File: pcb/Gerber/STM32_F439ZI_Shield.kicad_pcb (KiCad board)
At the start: 2 copper layers, 70 x 133.4 mm, 128 parts, among them CN10 Conn_02x17_Odd_Even, CN7 Conn_02x10_Odd_Even, CN8 Conn_02x08_Odd_Even, CN9 Conn_02x15_Odd_Even, J1 Conn_01x02_Pin, J3 Relais_Conn, J4 Conn_01x02_Pin, J5 Conn_01x02_Pin, J6 Conn_01x02_Pin, J7 Conn_01x02_Pin, J8 Conn_01x02_Pin, K1 G6S-2, K2 G6S-2, U1 LM2904, U10 LTV-817S, U11 LTV-817S, U12 FL25L16B, U13 R-78E-5.0-1.0, U15 ACS724xLCTR-05AB, U2 MAX3485, U3 LTV-817S, U4 LTV-817S, U5 LTV-817S, U6 LTV-817S, U7 LTV-817S, U8 LTV-817S, U9 LTV-817S

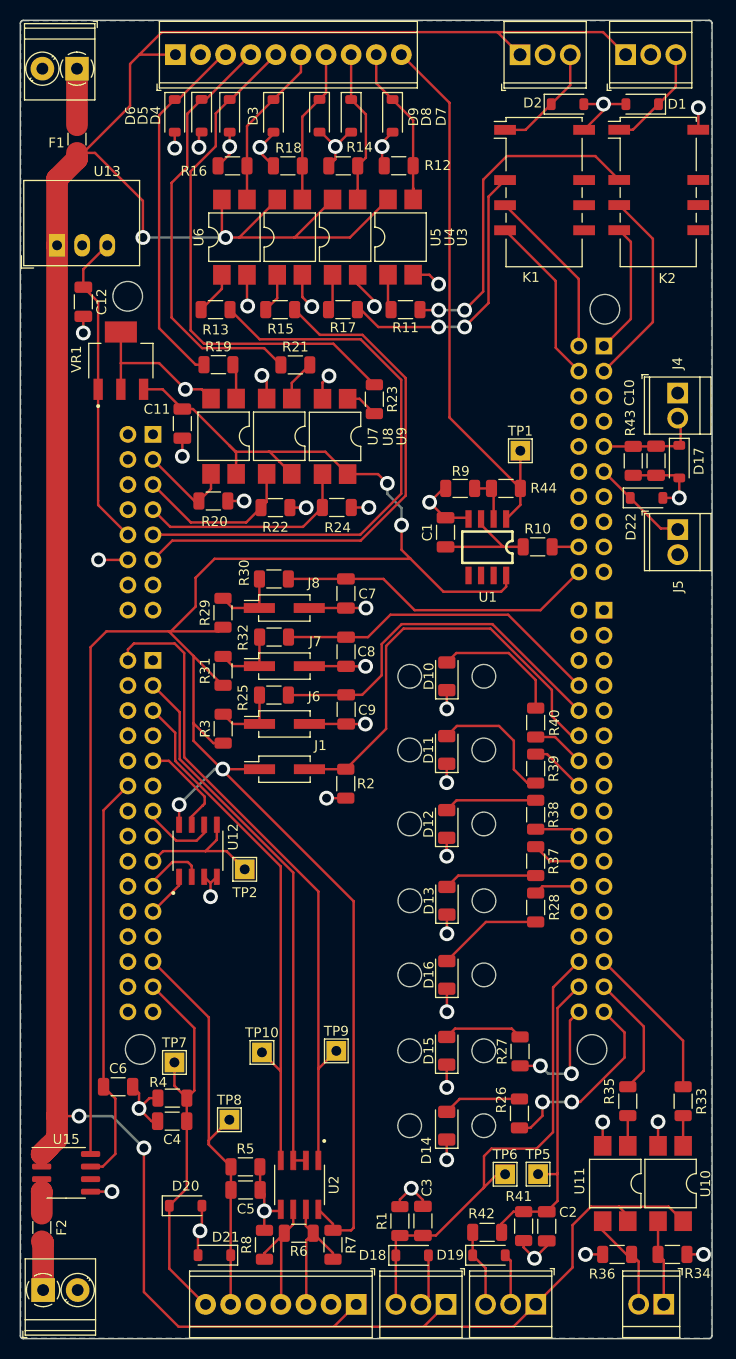
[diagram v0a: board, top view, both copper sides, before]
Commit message: finished assigning pins and creating pcb
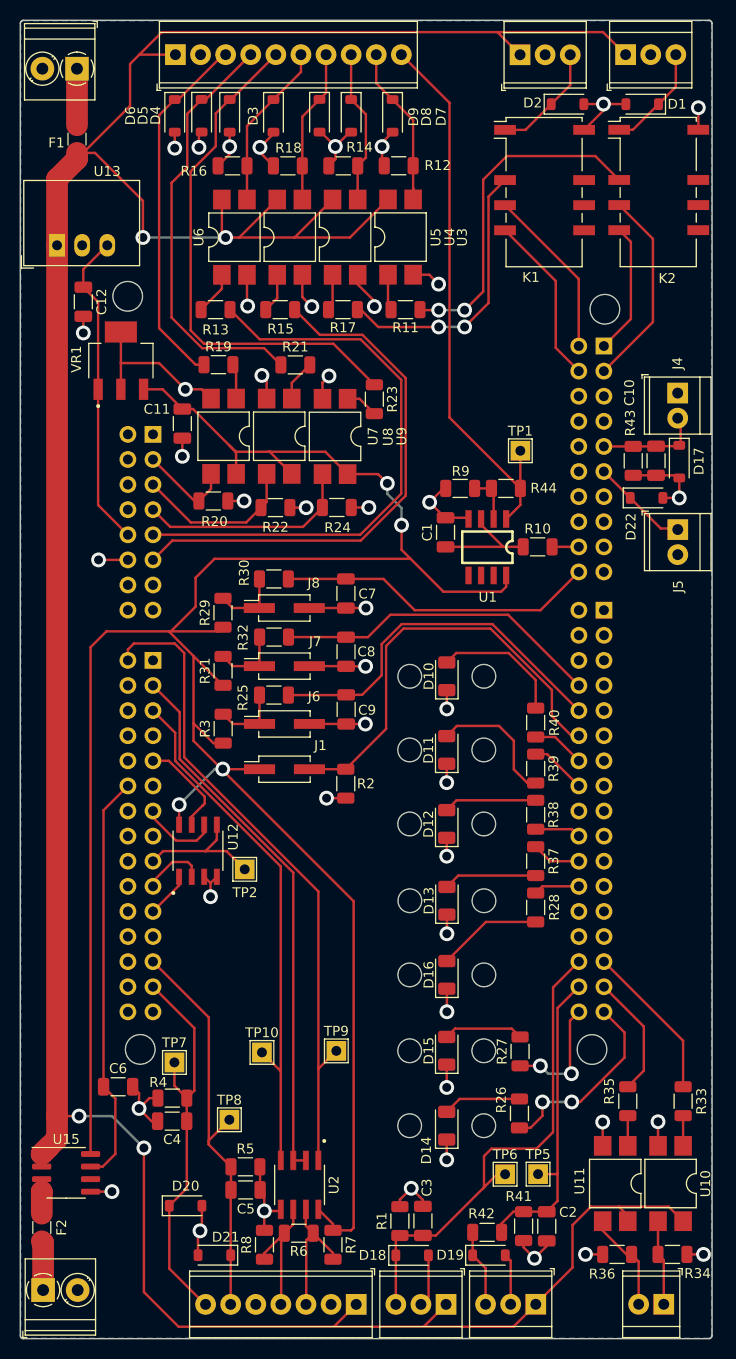
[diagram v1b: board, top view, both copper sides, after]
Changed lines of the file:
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@@
     (fp_circle (center 5.08 0) (end 6.18 0)
       (stroke (width 0.1) (type solid)) (fill none) (layer "F.Fab"))
-    (pad "1" thru_hole rect (at 0 0) (size 2.1 2.1) (drill 1.3) (layers "*.Cu" "*.Mask")
+    (pad "1" thru_hole rect (at 0 0) (size 2.1 2.1) (drill 1.1) (layers "*.Cu" "*.Mask")
       (net 1 "+24V") (pinfunction "Pin_1") (pintype "passive"))
-    (pad "2" thru_hole circle (at 2.54 0) (size 2.1 2.1) (drill 1.3) (layers "*.Cu" "*.Mask")
+    (pad "2" thru_hole circle (at 2.54 0) (size 2.1 2.1) (drill 1.1) (layers "*.Cu" "*.Mask")
       (net 2 "GND") (pinfunction "Pin_2") (pintype "passive"))
-    (pad "3" thru_hole circle (at 5.08 0) (size 2.1 2.1) (drill 1.3) (layers "*.Cu" "*.Mask")
+    (pad "3" thru_hole circle (at 5.08 0) (size 2.1 2.1) (drill 1.1) (layers "*.Cu" "*.Mask")
       (net 128 "/Endschalter/Endschalter_Hinten") (pinfunction "Pin_3") (pintype "passive"))
     (model "${KICAD6_3DMODEL_DIR}/TerminalBlock_TE-Connectivity.3dshapes/TerminalBlock_TE_282834-3_1x03_P2.54mm_Horizontal.wrl"
@@
     (fp_circle (center 2.54 0) (end 3.64 0)
       (stroke (width 0.1) (type solid)) (fill none) (layer "F.Fab"))
-    (pad "1" thru_hole rect (at 0 0 180) (size 2.1 2.1) (drill 1.3) (layers "*.Cu" "*.Mask")
+    (pad "1" thru_hole rect (at 0 0 180) (size 2.1 2.1) (drill 1.1) (layers "*.Cu" "*.Mask")
       (net 132 "/Optokoppler/Ext_Relais1_OUT") (pinfunction "Pin_1") (pintype "passive"))
-    (pad "2" thru_hole circle (at 2.54 0 180) (size 2.1 2.1) (drill 1.3) (layers "*.Cu" "*.Mask")
+    (pad "2" thru_hole circle (at 2.54 0 180) (size 2.1 2.1) (drill 1.1) (layers "*.Cu" "*.Mask")
       (net 133 "/Optokoppler/Ext_Relais2_OUT") (pinfunction "Pin_2") (pintype "passive"))
     (model "${KICAD6_3DMODEL_DIR}/TerminalBlock_TE-Connectivity.3dshapes/TerminalBlock_TE_282834-2_1x02_P2.54mm_Horizontal.wrl"
@@
     (fp_circle (center 5.08 0) (end 6.18 0)
       (stroke (width 0.1) (type solid)) (fill none) (layer "F.Fab"))
-    (pad "1" thru_hole rect (at 0 0 180) (size 2.1 2.1) (drill 1.3) (layers "*.Cu" "*.Mask")
+    (pad "1" thru_hole rect (at 0 0 180) (size 2.1 2.1) (drill 1.1) (layers "*.Cu" "*.Mask")
       (net 1 "+24V") (pinfunction "Pin_1") (pintype "passive"))
-    (pad "2" thru_hole circle (at 2.54 0 180) (size 2.1 2.1) (drill 1.3) (layers "*.Cu" "*.Mask")
+    (pad "2" thru_hole circle (at 2.54 0 180) (size 2.1 2.1) (drill 1.1) (layers "*.Cu" "*.Mask")
       (net 2 "GND") (pinfunction "Pin_2") (pintype "passive"))
-    (pad "3" thru_hole circle (at 5.08 0 180) (size 2.1 2.1) (drill 1.3) (layers "*.Cu" "*.Mask")
+    (pad "3" thru_hole circle (at 5.08 0 180) (size 2.1 2.1) (drill 1.1) (layers "*.Cu" "*.Mask")
       (net 150 "Net-(D19-K)") (pinfunction "Pin_3") (pintype "passive"))
     (model "${KICAD6_3DMODEL_DIR}/TerminalBlock_TE-Connectivity.3dshapes/TerminalBlock_TE_282834-3_1x03_P2.54mm_Horizontal.wrl"
@@
     (fp_circle (center 2.54 0) (end 3.64 0)
       (stroke (width 0.1) (type solid)) (fill none) (layer "F.Fab"))
-    (pad "1" thru_hole rect (at 0 0 270) (size 2.1 2.1) (drill 1.3) (layers "*.Cu" "*.Mask")
+    (pad "1" thru_hole rect (at 0 0 270) (size 2.1 2.1) (drill 1.1) (layers "*.Cu" "*.Mask")
       (net 53 "/STM32F439ZI/Opt_Analog_IN") (pinfunction "Pin_1") (pintype "passive"))
-    (pad "2" thru_hole circle (at 2.54 0 270) (size 2.1 2.1) (drill 1.3) (layers "*.Cu" "*.Mask")
+    (pad "2" thru_hole circle (at 2.54 0 270) (size 2.1 2.1) (drill 1.1) (layers "*.Cu" "*.Mask")
       (net 2 "GND") (pinfunction "Pin_2") (pintype "passive"))
     (model "${KICAD6_3DMODEL_DIR}/TerminalBlock_TE-Connectivity.3dshapes/TerminalBlock_TE_282834-2_1x02_P2.54mm_Horizontal.wrl"
@@
     (fp_circle (center 2.54 0) (end 3.64 0)
       (stroke (width 0.1) (type solid)) (fill none) (layer "F.Fab"))
-    (pad "1" thru_hole rect (at 0 0 270) (size 2.1 2.1) (drill 1.3) (layers "*.Cu" "*.Mask")
+    (pad "1" thru_hole rect (at 0 0 270) (size 2.1 2.1) (drill 1.1) (layers "*.Cu" "*.Mask")
       (net 2 "GND") (pinfunction "Pin_1") (pintype "passive"))
-    (pad "2" thru_hole circle (at 2.54 0 270) (size 2.1 2.1) (drill 1.3) (layers "*.Cu" "*.Mask")
+    (pad "2" thru_hole circle (at 2.54 0 270) (size 2.1 2.1) (drill 1.1) (layers "*.Cu" "*.Mask")
       (net 29 "/STM32F439ZI/Opt_Temperaturmessung") (pinfunction "Pin_2") (pintype "passive"))
     (model "${KICAD6_3DMODEL_DIR}/TerminalBlock_TE-Connectivity.3dshapes/TerminalBlock_TE_282834-2_1x02_P2.54mm_Horizontal.wrl"
@@
     (fp_circle (center 5.08 0) (end 6.18 0)
       (stroke (width 0.1) (type solid)) (fill none) (layer "F.Fab"))
-    (pad "1" thru_hole rect (at 0 0) (size 2.1 2.1) (drill 1.3) (layers "*.Cu" "*.Mask")
+    (pad "1" thru_hole rect (at 0 0) (size 2.1 2.1) (drill 1.1) (layers "*.Cu" "*.Mask")
       (net 1 "+24V") (pinfunction "Pin_1") (pintype "passive"))
-    (pad "2" thru_hole circle (at 2.54 0) (size 2.1 2.1) (drill 1.3) (layers "*.Cu" "*.Mask")
+    (pad "2" thru_hole circle (at 2.54 0) (size 2.1 2.1) (drill 1.1) (layers "*.Cu" "*.Mask")
       (net 2 "GND") (pinfunction "Pin_2") (pintype "passive"))
-    (pad "3" thru_hole circle (at 5.08 0) (size 2.1 2.1) (drill 1.3) (layers "*.Cu" "*.Mask")
+    (pad "3" thru_hole circle (at 5.08 0) (size 2.1 2.1) (drill 1.1) (layers "*.Cu" "*.Mask")
       (net 123 "/Endschalter/Endschalter_Vorne") (pinfunction "Pin_3") (pintype "passive"))
     (model "${KICAD6_3DMODEL_DIR}/TerminalBlock_TE-Connectivity.3dshapes/TerminalBlock_TE_282834-3_1x03_P2.54mm_Horizontal.wrl"
@@
     (fp_circle (center 5.08 0) (end 6.18 0)
       (stroke (width 0.1) (type solid)) (fill none) (layer "F.Fab"))
-    (pad "1" thru_hole rect (at 0 0 180) (size 2.1 2.1) (drill 1.3) (layers "*.Cu" "*.Mask")
+    (pad "1" thru_hole rect (at 0 0 180) (size 2.1 2.1) (drill 1.1) (layers "*.Cu" "*.Mask")
       (net 1 "+24V") (pinfunction "Pin_1") (pintype "passive"))
-    (pad "2" thru_hole circle (at 2.54 0 180) (size 2.1 2.1) (drill 1.3) (layers "*.Cu" "*.Mask")
+    (pad "2" thru_hole circle (at 2.54 0 180) (size 2.1 2.1) (drill 1.1) (layers "*.Cu" "*.Mask")
       (net 2 "GND") (pinfunction "Pin_2") (pintype "passive"))
-    (pad "3" thru_hole circle (at 5.08 0 180) (size 2.1 2.1) (drill 1.3) (layers "*.Cu" "*.Mask")
+    (pad "3" thru_hole circle (at 5.08 0 180) (size 2.1 2.1) (drill 1.1) (layers "*.Cu" "*.Mask")
       (net 3 "/STM32F439ZI/Abstandsmessung_MCU") (pinfunction "Pin_3") (pintype "passive"))
     (model "${KICAD6_3DMODEL_DIR}/TerminalBlock_TE-Connectivity.3dshapes/TerminalBlock_TE_282834-3_1x03_P2.54mm_Horizontal.wrl"
